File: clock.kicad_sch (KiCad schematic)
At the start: 2 parts, among them J1 Conn_01x04

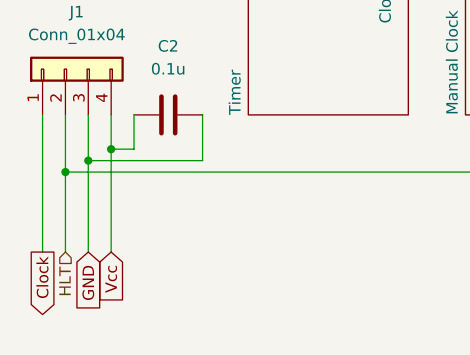
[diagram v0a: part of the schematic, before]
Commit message: Fix non standard switch buton
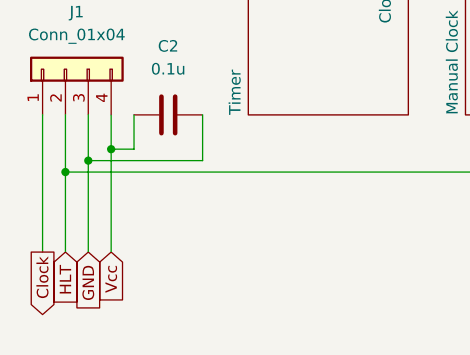
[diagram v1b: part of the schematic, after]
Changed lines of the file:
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@@
+    )
+  )
+  (global_label "HLT" (shape input) (at 73.66 80.01 270) (fields_autoplaced)
+    (effects (font (size 1.27 1.27)) (justify right))
+    (property "Intersheetrefs" "${INTERSHEET_REFS}" (at 73.66 86.3214 90)
+      (effects (font (size 1.27 1.27)) (justify right) hide)
     )
   )
@@
     )
   )
-  (hierarchical_label "HLT" (shape input) (at 73.66 80.01 270) (fields_autoplaced)
-    (effects (font (size 1.27 1.27)) (justify right))
-  )
   (symbol (lib_id "Device:C") (at 85.09 64.77 90) (unit 1)
